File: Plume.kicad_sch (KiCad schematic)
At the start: 0 parts

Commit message: Finished 65% of schematics
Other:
- note added: "Integrated Actuators Laboratory (LAI)"
- note added: "Logic - I2C Mux"
- note added: "MCU - Unit"
- note added: "Motor Control - Drivers"
- note added: "Power - Battery Management"
- note added: "Power - Path & Generation"
- note added: "Power - Wireless Receiver & USB"
- note added: "Revion History"
- note added: "Semester project: 02/2025 - 06/2025 Student: Théo Heng - theoheng@icloud.com Supervisors: Maël Dagon, Paolo Germano"
- note removed: "Random Sheet 1"
- note removed: "Random Sheet 2"
- note removed: "Revision History"

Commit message: Added footprints, images, almost finished all èages except for the MCU
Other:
- note added: "Misc - Mounting Holes & Fiducials"
- note added: "Motor Control - Driver 0"
- note added: "Motor Control - Driver 1"
- note added: "Motor Control - Driver 10"
- note added: "Motor Control - Driver 11"
- note added: "Motor Control - Driver 12"
- note added: "Motor Control - Driver 13"
- note added: "Motor Control - Driver 14"
- note added: "Motor Control - Driver 15"
- note added: "Motor Control - Driver 16"
- note added: "Motor Control - Driver 17"
- note added: "Motor Control - Driver 2"
- note added: "Motor Control - Driver 3"
- note added: "Motor Control - Driver 4"
- note added: "Motor Control - Driver 5"
- note added: "Motor Control - Driver 6"
- note added: "Motor Control - Driver 7"
- note added: "Motor Control - Driver 8"
- note added: "Motor Control - Driver 9"
- note added: "Revision History"
- note removed: "Revion History"
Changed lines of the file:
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@@
 		)
 	)
-	(text "..........................................."
+	(text "Motor Control - Driver 13"
 		(exclude_from_sim no)
 		(at 243.84 99.06 0)
@@
 		)
 	)
-	(text "Power - Sequencing"
+	(text "Motor Control - Driver 0"
 		(exclude_from_sim no)
 		(at 45.72 152.4 0)
@@
 		)
 	)
-	(text "..........................................."
+	(text "Motor Control - Driver 6"
 		(exclude_from_sim no)
 		(at 144.78 121.92 0)
@@
 		)
 	)
-	(text "..........................................."
+	(text "Revision History"
 		(exclude_from_sim no)
 		(at 243.84 152.4 0)
@@
 		)
 	)
-	(text "..........................................."
+	(text "Motor Control - Driver 3"
 		(exclude_from_sim no)
 		(at 144.78 99.06 0)
@@
 		)
 	)
-	(text "..........................................."
+	(text "Motor Control - Driver 17"
 		(exclude_from_sim no)
 		(at 243.84 129.54 0)
@@
 		)
 	)
-	(text "..........................................."
+	(text "Motor Control - Driver 14"
 		(exclude_from_sim no)
 		(at 243.84 106.68 0)
@@
 		)
 	)
-	(text "..........................................."
+	(text "Power - Sequencing"
 		(exclude_from_sim no)
 		(at 243.84 144.78 0)
@@
 		)
 	)
-	(text "..........................................."
+	(text "Motor Control - Driver 12"
 		(exclude_from_sim no)
 		(at 243.84 91.44 0)
@@
 		)
 	)
-	(text "..........................................."
+	(text "Motor Control - Driver 9"
 		(exclude_from_sim no)
 		(at 144.78 144.78 0)
@@
 		)
 	)
-	(text "Revion History"
+	(text "Motor Control - Driver 1"
 		(exclude_from_sim no)
 		(at 144.78 83.82 0)
@@
 		)
 	)
-	(text "..........................................."
+	(text "Motor Control - Driver 7"
 		(exclude_from_sim no)
 		(at 144.78 129.54 0)
@@
 		)
 	)
-	(text "..........................................."
+	(text "Misc - Mounting Holes & Fiducials"
 		(exclude_from_sim no)
 		(at 243.84 137.16 0)
@@
 		)
 	)
-	(text "..........................................."
+	(text "Motor Control - Driver 5"
 		(exclude_from_sim no)
 		(at 144.78 114.3 0)
@@
 		)
 	)
-	(text "..........................................."
+	(text "Motor Control - Driver 16"
 		(exclude_from_sim no)
 		(at 243.84 121.92 0)
@@
 		)
 	)
-	(text "..........................................."
+	(text "Motor Control - Driver 4"
 		(exclude_from_sim no)
 		(at 144.78 106.68 0)
@@
 		)
 	)
-	(text "..........................................."
+	(text "Motor Control - Driver 15"
 		(exclude_from_sim no)
 		(at 243.84 114.3 0)
@@
 		)
 	)
-	(text "..........................................."
+	(text "Motor Control - Driver 8"
 		(exclude_from_sim no)
 		(at 144.78 137.16 0)
@@
 		)
 	)
-	(text "..........................................."
+	(text "Motor Control - Driver 10"
 		(exclude_from_sim no)
 		(at 144.78 152.4 0)
@@
 		)
 	)
-	(text "..........................................."
+	(text "Motor Control - Driver 2"
 		(exclude_from_sim no)
 		(at 144.78 91.44 0)
@@
 		)
 	)
-	(text "..........................................."
+	(text "Motor Control - Driver 11"
 		(exclude_from_sim no)
 		(at 243.84 83.82 0)
@@
 			"AAAAAAAAAAAAAAAAAAAAAAAAAAAAAAAAAAAAAAAAAAAAAAAAAAAAAAAAAAAAAAAAAAAAAAAAAAAA"
 			"AAAAAAAAAAAAAAAAAAAAAAAAAAAAAAAAAAAAAAAAAAAAAAAAAAAAAAAAAAAAAAAAAAAAAAAAAAAA"
+			"AAAAAAAAAAAAAAAAAAAAAAAAAAAAAAAAAAAAAAAAAAAAAAAAAAAAAAAAAAAAAAAAAAAAAAAAAAAA"
+			"AAAAAAAAAAAAAAAAAAAAAAAAAAAAAAAAAAAAAAAAAAAAAAAAAAAAAAAAAAAAAAAAAAAAAAAAAAAA"
+			"AAAAAAAAAAAAAAAAAAAAAAAAAAAAAAAAAAAAAAAAAAAAAAAAAAAAAAAAAAAAAAAAAAAAAAAAAAAA"
+			"AAAAAAAAAAAAAAAAAAAAAAAAAAAAAAAAAAAAAAAAAAAAAAAAAAAAAAAAAAAAAAAAAAAAAAAAAAAA"
+			"AAAAAAAAAAAAAAAAAAAAAAAAAAAAAAAAAAAAAAAAAAAAAAAAAAAAAAAAAAAAAAAAAAAAAAAAAAAA"
+			"AAAAAAAAAAAAAAAAAAAAAAAAAAAAAAAAAAAAAAAAAAAAAAAAAAAAAAAAAAAAAAAAAAAAAAAAAAAA"
+			"AAAAAAAAAAAAAAAAAAAAAAAAAAAAAAAAAAAAAAAAAAAAAAAAAAAAAAAAAAAAAAAAAAAAAAAAAAAA"
+			"AAAAAAAAAAAAAAAAAAAAAAAAAAAAAAAAAAAAAAAAAAAAAAAAAAAAAAAAAAAAAAAAAAAAAAAAAAAA"
+			"AAAAAAAAAAAAAAAAAAAAAAAAAAAAAAAAAAAAAAAAAAAAAAAAAAAAAAAAAAAAAAAAAAAAAAAAAAAA"
+			"AAAAAAAAAAAAAAAAAAAAAAAAAAAAAAAAAAAAAAAAAAAAAAAAAAAAAAAAAAAAAAAAAAAAAAAAAAAA"
+			"AAAAAAAAAAAAAAAAAAAAAAAAAAAAAAAAAAAAAAAAAAAAAAAAAAAAAAAAAAAAAAAAAAAAAAAAAAAA"
+			"AAAAAAAAAAAAAAAAAAAAAAAAAAAAAAAAAAAAAAAAAAAAAAAAAAAAAAAAAAAAAAAAAAAAAAAAAAAA"
+			"AAAAAAAAAAAAAAAAAAAAAAAAAAAAAAAAAAAAAAAAAAAAAAAAAAAAAAAAAAAAAAAAAAAAAAAAAAAA"
+			"AAAAAAAAAAAAAAAAAAAAAAAAAAAAAAAAAAAAAAAAAAAAAAAAAAAAAAAAAAAAAAAAAAAAAAAAAAAA"
+			"AAAAAAAAAAAAAAAAAAAAAAAAAAAAAAAAAAAAAAAAAAAAAAAAAAAAAAAAAAAAAAAAAAAAAAAAAAAA"
+			"AAAAAAAAAAAAAAAAAAAAAAAAAAAAAAAAAAAAAAAAAAAAAAAAAAAAAAAAAAAAAAAAAAAAAAAAAAAA"
+			"AAAAAAAAAAAAAAAAAAAAAAAAAAAAAAAAAAAAAAAAAAAAAAAAAAAAAAAAAAAAAAAAAAAAAAAAAAAA"
+			"AAAAAAAAAAAAAAAAAAAAAAAAAAAAAAAAAAAAAAAAAAAAAAAAAAAAAAAAAAAAAAAAAAAAAAAAAAAA"
 			"AAAAAAAAAAAAAAAAAAAAAAAAAAAAAAAAAAAAAAAAAAAAAAAAAAAAAA=="
 		)
@@
 			(project "Plume"
 				(path "/0650c7a8-acba-429c-9f8e-eec0baf0bc1c"
-					(page "40")
+					(page "29")
 				)
 			)
@@
 			(project "Plume"
 				(path "/0650c7a8-acba-429c-9f8e-eec0baf0bc1c"
-					(page "41")
+					(page "30")
 				)
 			)

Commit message: Added RGB LED, added motor connectors, added test points, imported all 3D models
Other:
- note added: "User - RGB LED Indicator"
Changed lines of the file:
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@@
 		)
 	)
-	(text "Revision History"
+	(text "Power - Sequencing"
 		(exclude_from_sim no)
 		(at 243.84 152.4 0)
@@
 		)
 	)
-	(text "Power - Sequencing"
+	(text "Misc - Mounting Holes & Fiducials"
 		(exclude_from_sim no)
 		(at 243.84 144.78 0)
@@
 		)
 	)
-	(text "Misc - Mounting Holes & Fiducials"
+	(text "User - RGB LED Indicator"
 		(exclude_from_sim no)
 		(at 243.84 137.16 0)
@@
 		)
 	)
-	(text "..........................................."
+	(text "Revision History"
 		(exclude_from_sim no)
 		(at 342.9 83.82 0)
@@
 			"AAAAAAAAAAAAAAAAAAAAAAAAAAAAAAAAAAAAAAAAAAAAAAAAAAAAAAAAAAAAAAAAAAAAAAAAAAAA"
 			"AAAAAAAAAAAAAAAAAAAAAAAAAAAAAAAAAAAAAAAAAAAAAAAAAAAAAAAAAAAAAAAAAAAAAAAAAAAA"
+			"AAAAAAAAAAAAAAAAAAAAAAAAAAAAAAAAAAAAAAAAAAAAAAAAAAAAAAAAAAAAAAAAAAAAAAAAAAAA"
+			"AAAAAAAAAAAAAAAAAAAAAAAAAAAAAAAAAAAAAAAAAAAAAAAAAAAAAAAAAAAAAAAAAAAAAAAAAAAA"
+			"AAAAAAAAAAAAAAAAAAAAAAAAAAAAAAAAAAAAAAAAAAAAAAAAAAAAAAAAAAAAAAAAAAAAAAAAAAAA"
+			"AAAAAAAAAAAAAAAAAAAAAAAAAAAAAAAAAAAAAAAAAAAAAAAAAAAAAAAAAAAAAAAAAAAAAAAAAAAA"
+			"AAAAAAAAAAAAAAAAAAAAAAAAAAAAAAAAAAAAAAAAAAAAAAAAAAAAAAAAAAAAAAAAAAAAAAAAAAAA"
+			"AAAAAAAAAAAAAAAAAAAAAAAAAAAAAAAAAAAAAAAAAAAAAAAAAAAAAAAAAAAAAAAAAAAAAAAAAAAA"
+			"AAAAAAAAAAAAAAAAAAAAAAAAAAAAAAAAAAAAAAAAAAAAAAAAAAAAAAAAAAAAAAAAAAAAAAAAAAAA"
+			"AAAAAAAAAAAAAAAAAAAAAAAAAAAAAAAAAAAAAAAAAAAAAAAAAAAAAAAAAAAAAAAAAAAAAAAAAAAA"
+			"AAAAAAAAAAAAAAAAAAAAAAAAAAAAAAAAAAAAAAAAAAAAAAAAAAAAAAAAAAAAAAAAAAAAAAAAAAAA"
+			"AAAAAAAAAAAAAAAAAAAAAAAAAAAAAAAAAAAAAAAAAAAAAAAAAAAAAAAAAAAAAAAAAAAAAAAAAAAA"
+			"AAAAAAAAAAAAAAAAAAAAAAAAAAAAAAAAAAAAAAAAAAAAAAAAAAAAAAAAAAAAAAAAAAAAAAAAAAAA"
+			"AAAAAAAAAAAAAAAAAAAAAAAAAAAAAAAAAAAAAAAAAAAAAAAAAAAAAAAAAAAAAAAAAAAAAAAAAAAA"
+			"AAAAAAAAAAAAAAAAAAAAAAAAAAAAAAAAAAAAAAAAAAAAAAAAAAAAAAAAAAAAAAAAAAAAAAAAAAAA"
+			"AAAAAAAAAAAAAAAAAAAAAAAAAAAAAAAAAAAAAAAAAAAAAAAAAAAAAAAAAAAAAAAAAAAAAAAAAAAA"
+			"AAAAAAAAAAAAAAAAAAAAAAAAAAAAAAAAAAAAAAAAAAAAAAAAAAAAAAAAAAAAAAAAAAAAAAAAAAAA"
+			"AAAAAAAAAAAAAAAAAAAAAAAAAAAAAAAAAAAAAAAAAAAAAAAAAAAAAAAAAAAAAAAAAAAAAAAAAAAA"
+			"AAAAAAAAAAAAAAAAAAAAAAAAAAAAAAAAAAAAAAAAAAAAAAAAAAAAAAAAAAAAAAAAAAAAAAAAAAAA"
+			"AAAAAAAAAAAAAAAAAAAAAAAAAAAAAAAAAAAAAAAAAAAAAAAAAAAAAAAAAAAAAAAAAAAAAAAAAAAA"
 			"AAAAAAAAAAAAAAAAAAAAAAAAAAAAAAAAAAAAAAAAAAAAAAAAAAAAAA=="
 		)
@@
 			(project "Plume"
 				(path "/0650c7a8-acba-429c-9f8e-eec0baf0bc1c"
-					(page "29")
+					(page "30")
 				)
 			)
@@
 			(project "Plume"
 				(path "/0650c7a8-acba-429c-9f8e-eec0baf0bc1c"
-					(page "30")
+					(page "31")
 				)
 			)

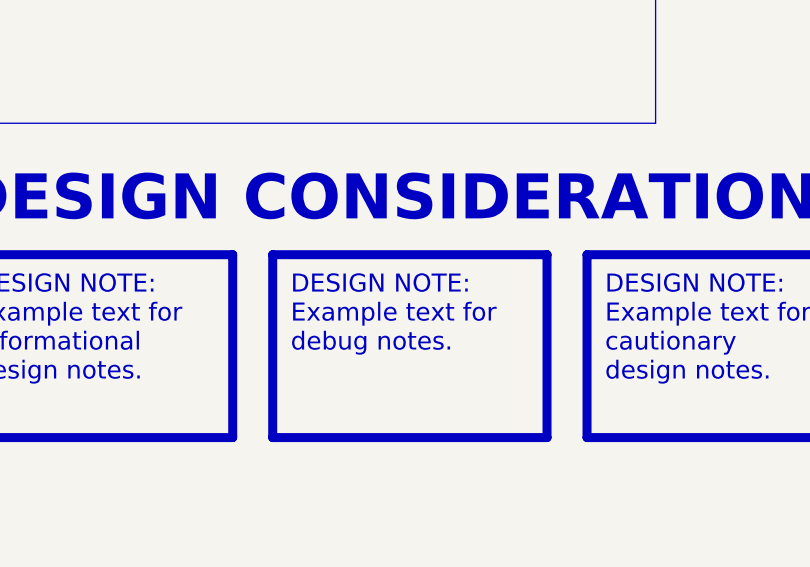
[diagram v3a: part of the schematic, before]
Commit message: Finished schematic, imported all footprints, all 3D models and created STM32 project, now need to proofread shematic before layout
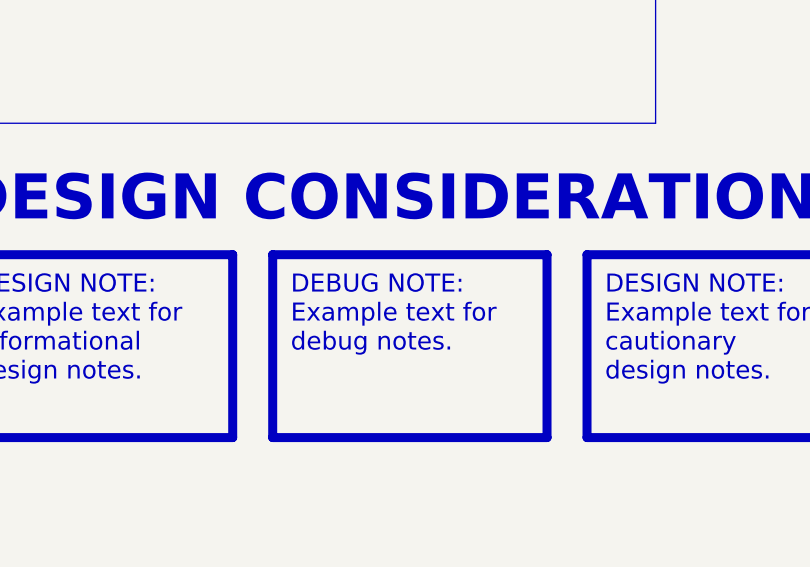
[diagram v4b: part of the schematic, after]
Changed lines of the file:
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@@
 		)
 	)
-	(text_box "DESIGN NOTE:\nExample text for debug notes."
+	(text_box "DEBUG NOTE:\nExample text for debug notes."
 		(exclude_from_sim no)
 		(at 61.595 258.445 0)
@@
 			"AAAAAAAAAAAAAAAAAAAAAAAAAAAAAAAAAAAAAAAAAAAAAAAAAAAAAAAAAAAAAAAAAAAAAAAAAAAA"
 			"AAAAAAAAAAAAAAAAAAAAAAAAAAAAAAAAAAAAAAAAAAAAAAAAAAAAAAAAAAAAAAAAAAAAAAAAAAAA"
+			"AAAAAAAAAAAAAAAAAAAAAAAAAAAAAAAAAAAAAAAAAAAAAAAAAAAAAAAAAAAAAAAAAAAAAAAAAAAA"
+			"AAAAAAAAAAAAAAAAAAAAAAAAAAAAAAAAAAAAAAAAAAAAAAAAAAAAAAAAAAAAAAAAAAAAAAAAAAAA"
+			"AAAAAAAAAAAAAAAAAAAAAAAAAAAAAAAAAAAAAAAAAAAAAAAAAAAAAAAAAAAAAAAAAAAAAAAAAAAA"
+			"AAAAAAAAAAAAAAAAAAAAAAAAAAAAAAAAAAAAAAAAAAAAAAAAAAAAAAAAAAAAAAAAAAAAAAAAAAAA"
+			"AAAAAAAAAAAAAAAAAAAAAAAAAAAAAAAAAAAAAAAAAAAAAAAAAAAAAAAAAAAAAAAAAAAAAAAAAAAA"
+			"AAAAAAAAAAAAAAAAAAAAAAAAAAAAAAAAAAAAAAAAAAAAAAAAAAAAAAAAAAAAAAAAAAAAAAAAAAAA"
+			"AAAAAAAAAAAAAAAAAAAAAAAAAAAAAAAAAAAAAAAAAAAAAAAAAAAAAAAAAAAAAAAAAAAAAAAAAAAA"
+			"AAAAAAAAAAAAAAAAAAAAAAAAAAAAAAAAAAAAAAAAAAAAAAAAAAAAAAAAAAAAAAAAAAAAAAAAAAAA"
+			"AAAAAAAAAAAAAAAAAAAAAAAAAAAAAAAAAAAAAAAAAAAAAAAAAAAAAAAAAAAAAAAAAAAAAAAAAAAA"
+			"AAAAAAAAAAAAAAAAAAAAAAAAAAAAAAAAAAAAAAAAAAAAAAAAAAAAAAAAAAAAAAAAAAAAAAAAAAAA"
+			"AAAAAAAAAAAAAAAAAAAAAAAAAAAAAAAAAAAAAAAAAAAAAAAAAAAAAAAAAAAAAAAAAAAAAAAAAAAA"
+			"AAAAAAAAAAAAAAAAAAAAAAAAAAAAAAAAAAAAAAAAAAAAAAAAAAAAAAAAAAAAAAAAAAAAAAAAAAAA"
+			"AAAAAAAAAAAAAAAAAAAAAAAAAAAAAAAAAAAAAAAAAAAAAAAAAAAAAAAAAAAAAAAAAAAAAAAAAAAA"
+			"AAAAAAAAAAAAAAAAAAAAAAAAAAAAAAAAAAAAAAAAAAAAAAAAAAAAAAAAAAAAAAAAAAAAAAAAAAAA"
+			"AAAAAAAAAAAAAAAAAAAAAAAAAAAAAAAAAAAAAAAAAAAAAAAAAAAAAAAAAAAAAAAAAAAAAAAAAAAA"
+			"AAAAAAAAAAAAAAAAAAAAAAAAAAAAAAAAAAAAAAAAAAAAAAAAAAAAAAAAAAAAAAAAAAAAAAAAAAAA"
+			"AAAAAAAAAAAAAAAAAAAAAAAAAAAAAAAAAAAAAAAAAAAAAAAAAAAAAAAAAAAAAAAAAAAAAAAAAAAA"
+			"AAAAAAAAAAAAAAAAAAAAAAAAAAAAAAAAAAAAAAAAAAAAAAAAAAAAAAAAAAAAAAAAAAAAAAAAAAAA"
+			"AAAAAAAAAAAAAAAAAAAAAAAAAAAAAAAAAAAAAAAAAAAAAAAAAAAAAAAAAAAAAAAAAAAAAAAAAAAA"
+			"AAAAAAAAAAAAAAAAAAAAAAAAAAAAAAAAAAAAAAAAAAAAAAAAAAAAAAAAAAAAAAAAAAAAAAAAAAAA"
+			"AAAAAAAAAAAAAAAAAAAAAAAAAAAAAAAAAAAAAAAAAAAAAAAAAAAAAAAAAAAAAAAAAAAAAAAAAAAA"
+			"AAAAAAAAAAAAAAAAAAAAAAAAAAAAAAAAAAAAAAAAAAAAAAAAAAAAAAAAAAAAAAAAAAAAAAAAAAAA"
+			"AAAAAAAAAAAAAAAAAAAAAAAAAAAAAAAAAAAAAAAAAAAAAAAAAAAAAAAAAAAAAAAAAAAAAAAAAAAA"
+			"AAAAAAAAAAAAAAAAAAAAAAAAAAAAAAAAAAAAAAAAAAAAAAAAAAAAAAAAAAAAAAAAAAAAAAAAAAAA"
+			"AAAAAAAAAAAAAAAAAAAAAAAAAAAAAAAAAAAAAAAAAAAAAAAAAAAAAAAAAAAAAAAA/////wAAAAAA"
+			"AAAAAAAAAAAAAAAAAAAAAAAAAAAAAAAAAAAAAAAAAAAAAAAAAAAAAAAAAAAAAAAAAAAAAAAAAAAA"
+			"AAAAAAAAAAAAAAAAAAAAAAAAAAAAAAAAAAAAAAAAAAAAAAAAAAAAAAAAAAAAAAAAAAAAAAAAAAAA"
+			"AAAAAAAAAAAAAAAAAAAAAAAAAAAAAAAAAAAAAAAAAAAAAAAAAAAAAAAAAAAAAAAAAAAAAAAAAAAA"
+			"AAAAAAAAAAAAAAAAAAAAAAAAAAAAAAAAAAAAAAAAAAAAAAAAAAAAAAAAAAAAAAAAAAAAAAAAAAAA"
+			"AAAAAAAAAAAAAAAAAAAAAAAAAAAAAAAAAAAAAAAAAAAAAAAAAAAAAAAAAAAAAAAAAAAAAAAAAAAA"
+			"AAAAAAAAAAAAAAAAAAAAAAAAAAAAAAAAAAAAAAAAAAAAAAAAAAAAAAAAAAAAAAAAAAAAAAAAAAAA"
+			"AAAAAAAAAAAAAAAAAAAAAAAAAAAAAAAAAAAAAAAAAAAAAAAAAAAAAAAAAAAAAAAAAAAAAAAAAAAA"
+			"AAAAAAAAAAAAAAAAAAAAAAAAAAAAAAAAAAAAAAAAAAAAAAAAAAAAAAAAAAAAAAAAAAAAAAAAAAAA"
+			"AAAAAAAAAAAAAAAAAAAAAAAAAAAAAAAAAAAAAAAAAAAAAAAAAAAAAHEBdoKLAgEBCoH/AwAAAAFC"
+			"gIBxAnKB/wEBAQFBgIBxAXaCiwIBASeAgAIBdoKLAgECAVGAgAIBdoKLAgiCAwSCAgQAAQFQAHEB"
+			"doKLAgEBAoH/AwAAAAFRgIACAXaCiwIFggUEggQEAAEBUABxAXaCiwIBAQKB/wMAAAAAAUOAgHEB"
+			"doKMAgMBUYCAgn4BAXaCjAIEggEEggAEAAEBUABxAXaCjAIBCQqB/wMAAAABQoCAcQJygf8BAQEB"
+			"QYCAcQF2gowCAQEngIACAXaCjAIBAgFRgIACAXaCjAIIggMEggIEAAEBUABxAXaCjAIBCQKB/wMA"
+			"AAABUYCAAgF2gowCBYIFBIIEBAABAVAAcQF2gowCAQkCgf8DAAAAAAEzgIABBAMBAAyGgABAAgA/"
+			"hoAAQAYAP4aAAEACAHEBdoKPAgIBLYCAgiUEAXaCjwIIgv0DAYIlBAAIgv0DGQEjU01BQU1vdmNA"
+			"YnZlYzRAdmVjNEB2ZWM0AIIkBAMAAYImBACGgABAAgSCAQQEggEEAAAAAAAAAAE/AIaAAEAGCIID"
+			"BAiCAwQAAAAAAAAAAT8AhoAAQAIFggUEBYIFBAAAAAAAAAAAAwUAAAEshoAAQAKCJgQBdoKPAgSC"
+			"AQSCKgQBAAEshoAAQAY/AXaCjwIIggMEgisEAQABLIaAAEACPwF2go8CBYIFBIIsBAEAAUKAgHEC"
+			"coH/AAICAUGAgHEBdoKQAgEBK4CABAF2gpACAAUFASeAgIDPAXaCkAIAAgFRAIDPAXaCkAIEggEE"
+			"ggAEAAEAAVGAgIDPAXaCkAIEggEEgioEAAEBUABxAXaCkAIBIgyB/wMAAAABJ4CABAF2gpACAAIB"
+			"UQAEAXaCkAIIggMEggIEAAEAAVGAgAQBdoKQAgiCAwSCKwQAAQFQAHEBdoKQAgEiBIH/AwAAAAEn"
+			"gIAEAXaCkAIAAgFRAAQBdoKQAgWCBQSCBAQAAQABUYCABAF2gpACBYIFBIIsBAABAVAAcQF2gpAC"
+			"ASIEgf8DAAAAAU4AcQF2gpACCIL9A4L+AwABJ4CABAF2gpACAAKCOgQBUQAEAXaCkAIIggMEggIE"
+			"AAEAAUGAgHEBdoKRAgEBK4CABAF2gpECAAUFASeAgIDPAXaCkQIAAgFRAIDPAXaCkQIEggEEggAE"
+			"AAEAAVGAgIDPAXaCkQIEggEEgioEAAEBUABxAXaCkQIBcgyB/wMAAAABJ4CABAF2gpECAAIBUQAE"
+			"AXaCkQIIggMEggIEAAEAAVGAgAQBdoKRAgiCAwSCKwQAAQFQAHEBdoKRAgFyBIH/AwAAAAEngIAE"
+			"AXaCkQIAAgFRAAQBdoKRAgWCBQSCBAQAAQABUYCABAF2gpECBYIFBAAAAAAAAAAAAAAAAAAAAAAA"
+			"AAAAAAAAAAAAAAAAAAAAAAAAAAAAAAAAAAAAAAAAAAAAAAAAAAAAAAAAAAAAAAAAAAAAAAAAAAAA"
+			"AAAAAAAAAAAAAAAAAAAAAAAAAAAAAAAAAAAAAAAAAAAAAAAAAAAAAAAAAAAAAAAAAAAAAAAAAAAA"
+			"AAAAAAAAAAAAAAAAAAAAAAAAAAAAAAAAAAAAAAAAAAAAAAAAAAAAAAAAAAAAAAAAAAAAAAAAAAAA"
+			"AAAAAAAAAAAAAAAAAAAAAAAAAAAAAAAAAAAAAAAAAAAAAAAAAAAAAAAAAAAAAAAAAAAAAAAAAAAA"
+			"AAAAAAAAAAAAAAAAAAAAAAAAAAAAAAAAAAAAAAAAAAAAAAAAAAAAAAAAAAAAAAAAAAAAAAAAAAAA"
+			"AAAAAAAAAAAAAAAAAAAAAAAAAAAAAAAAAAAAAAAAAAAAAAAAAAAAAAAAAAAAAAAAAAAAAAAAAAAA"
+			"AAAAAAAAAAAAAAAAAAAAAAAAAAAAAAAAAAAAAAAAAAAAAAAAAAAAAAAAAAAAAAAAAAAAAAAAAAAA"
+			"AAAAAAAAAAAAAAAAAAAAAAAAAAAAAAAAAAAAAAAAAAAAAAAAAAAAAAAAAAAAAAAAAAAAAAAAAAAA"
+			"AAAAAAAAAAAAAAAAAAAAAAAAAAAAAAAAAAAAAAAAAAAAAAAAAAAAAAAAAAAAAAAAAAAAAAAAAAAA"
+			"AAAAAAAAAAAAAAAAAAAAAAAAAAAAAAAAAAAAAAAAAAAAAAAAAAAAAAAAAAAAAAAAAAAAAAAAAAAA"
+			"AAAAAAAAAAAAAAAAAAAAAAAAAAAAAAAAAAAAAAAAAAAAAAAAAAAAAAAAAAAAAAAAAAAAAAAAAAAA"
+			"AAAAAAAAAAAAAAAAAAAAAAAAAAAAAAAAAAAAAAAAAAAAAAAAAAAAAAAAAAAAAAAAAAAAAAAAAAAA"
+			"AAAAAAAAAAAAAAAAAAAAAAAAAAAAAAAAAAAAAAAAAAAAAAAAAAAAAAAAAAAAAAAAAAAAAAAAAAAA"
+			"AAAAAAAAAAAAAAAAAAAAAAAAAAAAAAAAAAAAAAAAAAAAAAAAAAAAAAAAAAAAAAAAAAAAAAAAAAAA"
+			"AAAAAAAAAAAAAAAAAAAAAAAAAAAAAAAAAAAAAAAAAAAAAAAAAAAAAAAAAAAAAAAAAAAAAAAAAAAA"
+			"AAAAAAAAAAAAAAAAAAAAAAAAAAAAAAAAAAAAAAAAAAAAAAAAAAAAAAAAAAAAAAAAAAAAAAAAAAAA"
+			"AAAAAAAAAAAAAAAAAAAAAAAAAAAAAAAAAAAAAAAAAAAAAAAAAAAAAAAAAAAAAAAAAAAAAAAAAAAA"
+			"AAAAAAAAAAAAAAAAAAAAAAAAAAAAAAAAAAAAAAAAAAAAAAAAAAAAAAAAH4AKAQAAALBE5EoBAAAA"
+			"sNkcFgEAAABwq4AKAQAAADCsgAoBAAAAUM14CgEAAABweXsKAQAAAHB5ewoBAAAAcHl7CgEAAACw"
+			"2RwWAQAAAHB5ewoBAAAAUM14CgEAAADgRORKAQAAAHB5ewoBAAAAEEXkSgEAAABwMeRKAQAAAAAf"
+			"gAoBAAAAQEXkSgEAAAAwNORKAQAAAHCrgAoBAAAAcEXkSgEAAACw43cKAQAAANCrgAoBAAAAsON3"
+			"CgEAAACw43cKAQAAALDjdwoBAAAAoEXkSgEAAADwk3cKAQAAANCrgAoBAAAA8JN3CgEAAADwk3cK"
+			"AQAAANBF5EoBAAAAMDLkSgEAAADQq4AKAQAAADAy5EoBAAAAMDLkSgEAAAAARuRKAQAAALAx5EoB"
+			"AAAAMKyACgEAAACwMeRKAQAAALAx5EoBAAAAUM14CgEAAABwMeRKAQAAAFDNeAoBAAAAMEbkSgEA"
+			"AADwMuRKAQAAAAAfgAoBAAAA8DLkSgEAAABgRuRKAQAAADA05EoBAAAAwB+ACgEAAADwMuRKAQAA"
+			"ADA05EoBAAAAMDTkSgEAAABwNORKAQAAAEDJ3UoBAAAAUM14CgEAAABAyd1KAQAAAEDJ3UoBAAAA"
+			"QMndSgEAAACQRuRKAQAAALA05EoBAAAAQMndSgEAAABQzXgKAQAAAEDJ3UoBAAAAwEbkSgEAAADw"
+			"NORKAQAAAJDJ3UoBAAAAcKuACgEAAADwRuRKAQAAALDjdwoBAAAAMKyACgEAAACw43cKAQAAALDj"
+			"dwoBAAAAsON3CgEAAACw43cKAQAAALDjdwoBAAAAsON3CgEAAACw43cKAQAAALDjdwoBAAAAsON3"
+			"CgEAAABgrIAKAQAAAFDNeAoBAAAAUM14CgEAAAAgR+RKAQAAAFBH5EoBAAAAsON3CgEAAABQzXgK"
+			"AQAAALDjdwoBAAAAUM14CgEAAACAR+RKAQAAADA15EoBAAAAAB+ACgEAAAAwNeRKAQAAALBH5EoB"
+			"AAAAsJh0CgEAAADAH4AKAQAAADA15EoBAAAAsJh0CgEAAACwmHQKAQAAAHA15EoBAAAAkMndSgEA"
+			"AABQzXgKAQAAAJDJ3UoBAAAAkMndSgEAAACQyd1KAQAAAOBH5EoBAAAAsDXkSgEAAACQyd1KAQAA"
+			"AFDNeAoBAAAAkMndSgEAAAAQSORKAQAAAPA15EoBAAAA4MndSgEAAABwq4AKAQAAAEBI5EoBAAAA"
+			"sON3CgEAAADQq4AKAQAAAHBI5EoBAAAAMMR2CgEAAADQq4AKAQAAAKBI5EoBAAAA8BrdSgEAAADQ"
+			"q4AKAQAAANBI5EoBAAAAMBvdSgEAAAAwrIAKAQAAADAb3UoBAAAAsAAAAAAAAAAAAAAAAAAAAAAA"
+			"AAAAAAAAAAAAAAAAAAAAAAAAAAAAAAAAAAAAAAAAAAAAAAAAAAAAAAAAAAAAAAAAAAAAAAAAAAAA"
+			"AAAAAAAAAAAAAAAAAAAAAAAAAAAAAAAAAAAAAAAAAAAAAAAAAAAAAAAAAAAAAAAAAAAAAAAAAAAA"

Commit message: Cleaned repo, cleaned and exported shematic, advanced rough layout
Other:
- note added: "KiCad Template by Vincent Nguyen"
- note added: "MULTIPLE MOTOR CONTROLLER WITH SENSORLESS POSITION CONTROL"
- note removed: "Add a comment here"
